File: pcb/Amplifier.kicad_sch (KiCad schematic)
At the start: 1 part, among them U6 MA12040PXUMA1

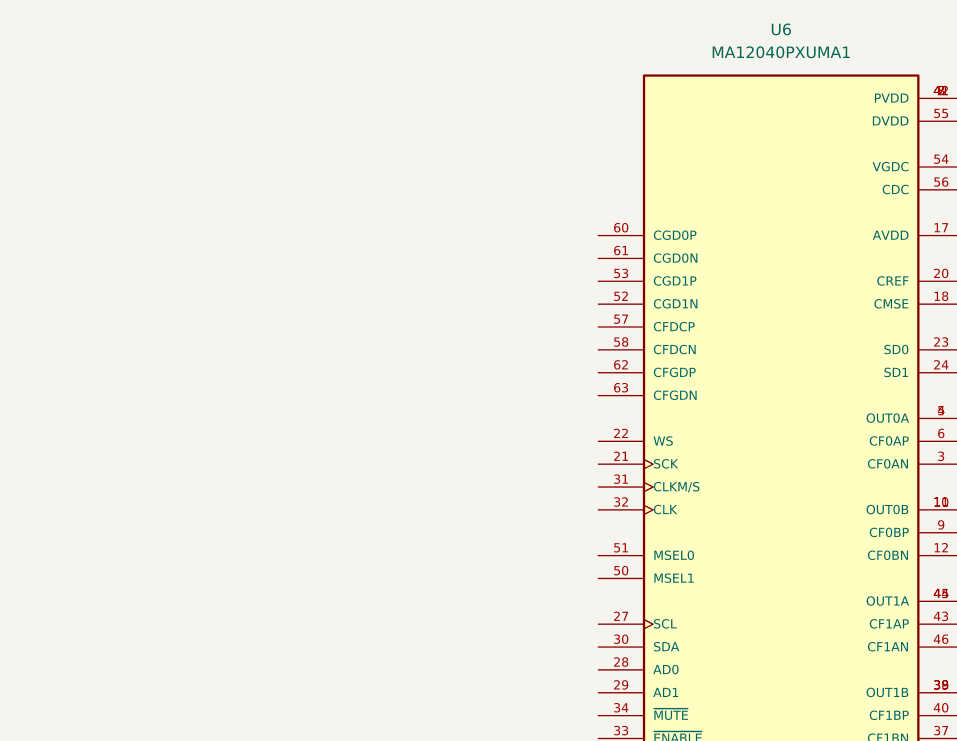
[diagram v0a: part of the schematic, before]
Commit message: - USB sound wired
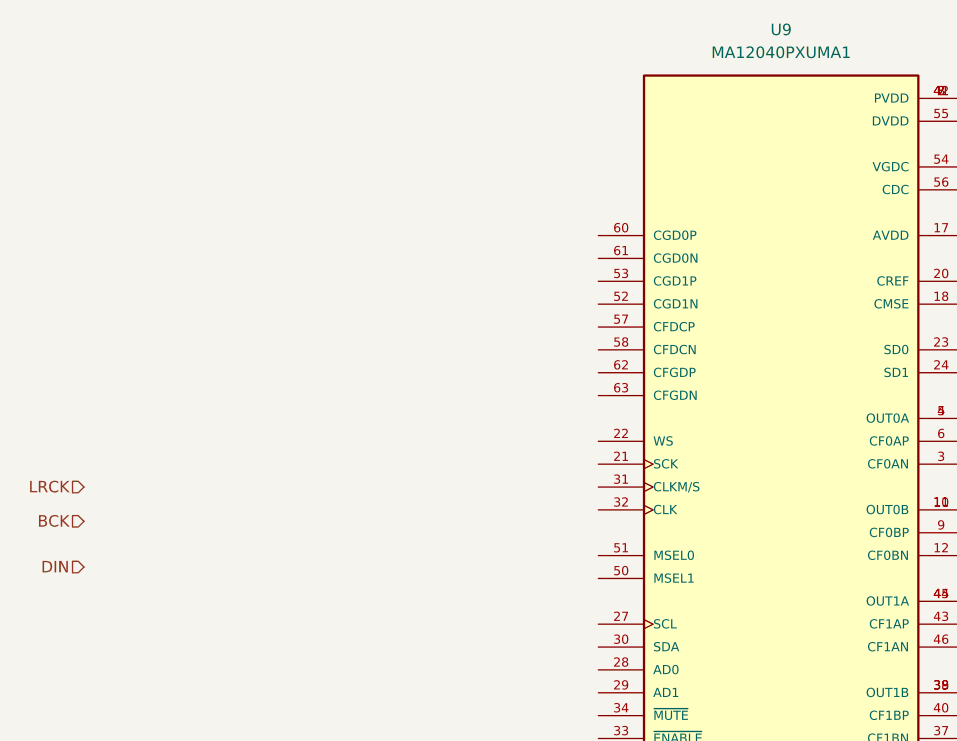
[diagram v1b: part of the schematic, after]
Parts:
- renumbered U6 to U9
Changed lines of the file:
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@@
 (kicad_sch (version 20230121) (generator eeschema)
   (paper "A4")
+  (hierarchical_label "DIN" (shape input) (at 48.26 105.41 180) (fields_autoplaced)
+    (effects (font (size 1.27 1.27)) (justify right))
+  )
+  (hierarchical_label "BCK" (shape input) (at 48.26 100.33 180) (fields_autoplaced)
+    (effects (font (size 1.27 1.27)) (justify right))
+  )
+  (hierarchical_label "LRCK" (shape input) (at 48.26 96.52 180) (fields_autoplaced)
+    (effects (font (size 1.27 1.27)) (justify right))
+  )
   (symbol (lib_id "MA12040PXUMA1:MA12040PXUMA1") (at 125.73 96.52 0) (unit 1)
     (in_bom yes) (on_board yes) (dnp no) (fields_autoplaced)
-    (property "Reference" "U6" (at 125.73 45.72 0)
+    (property "Reference" "U9" (at 125.73 45.72 0)
       (effects (font (size 1.27 1.27)))
     )
@@
       (project "VolumioAmp"
         (path "/c639bae0-d26f-43ee-9e8c-ca060284bd0b/ecbd0217-ab04-4196-9487-2acaa32ad17c"
-          (reference "U6") (unit 1)
+          (reference "U9") (unit 1)
         )
       )

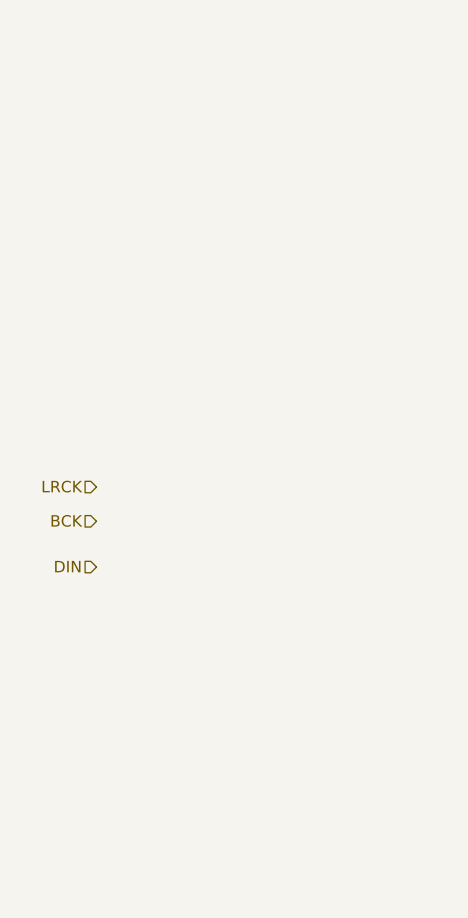
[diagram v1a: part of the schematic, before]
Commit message: WM8804 via i2c
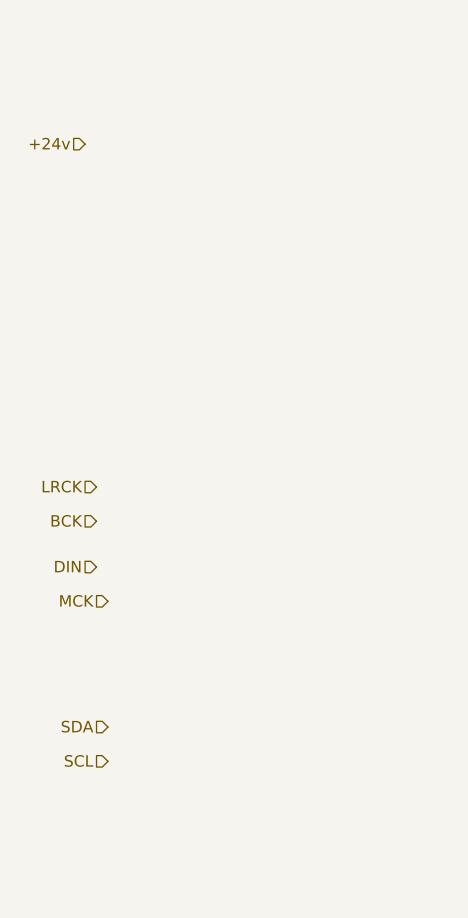
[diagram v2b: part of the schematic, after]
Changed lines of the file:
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@@
+    (effects (font (size 1.27 1.27)) (justify right))
+  )
+  (hierarchical_label "SDA" (shape input) (at 49.53 123.19 180) (fields_autoplaced)
     (effects (font (size 1.27 1.27)) (justify right))
   )
@@
     (effects (font (size 1.27 1.27)) (justify right))
   )
+  (hierarchical_label "SCL" (shape input) (at 49.53 127 180) (fields_autoplaced)
+    (effects (font (size 1.27 1.27)) (justify right))
+  )
+  (hierarchical_label "MCK" (shape input) (at 49.53 109.22 180) (fields_autoplaced)
+    (effects (font (size 1.27 1.27)) (justify right))
+  )
   (hierarchical_label "LRCK" (shape input) (at 48.26 96.52 180) (fields_autoplaced)
     (effects (font (size 1.27 1.27)) (justify right))
   )
+  (hierarchical_label "+24v" (shape input) (at 46.99 58.42 180) (fields_autoplaced)
+    (effects (font (size 1.27 1.27)) (justify right))
+  )

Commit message: - work in progress
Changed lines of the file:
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@@
 (kicad_sch (version 20230121) (generator eeschema)
   (paper "A4")
-  (hierarchical_label "DIN" (shape input) (at 48.26 105.41 180) (fields_autoplaced)
+  (bus (pts (xy 36.83 91.44) (xy 83.82 91.44))
+    (stroke (width 0) (type default))
+  )
+  (label "I2S{LRCK BCK MCK D}" (at 43.18 91.44 0) (fields_autoplaced)
+    (effects (font (size 1.27 1.27)) (justify left bottom))
+  )
+  (hierarchical_label "I2S" (shape input) (at 36.83 91.44 180) (fields_autoplaced)
     (effects (font (size 1.27 1.27)) (justify right))
   )
@@
     (effects (font (size 1.27 1.27)) (justify right))
   )
-  (hierarchical_label "BCK" (shape input) (at 48.26 100.33 180) (fields_autoplaced)
-    (effects (font (size 1.27 1.27)) (justify right))
-  )
   (hierarchical_label "SCL" (shape input) (at 49.53 127 180) (fields_autoplaced)
     (effects (font (size 1.27 1.27)) (justify right))
   )
-  (hierarchical_label "MCK" (shape input) (at 49.53 109.22 180) (fields_autoplaced)
-    (effects (font (size 1.27 1.27)) (justify right))
-  )
-  (hierarchical_label "LRCK" (shape input) (at 48.26 96.52 180) (fields_autoplaced)
-    (effects (font (size 1.27 1.27)) (justify right))
-  )

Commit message: - voor aanpassing design rules jclpcb
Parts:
- U9: footprint Libraries:QFN50P900X900X90-65N -> Footprints:QFN50P900X900X90-65N
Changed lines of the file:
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@@
       (effects (font (size 1.27 1.27)))
     )
-    (property "Footprint" "Libraries:QFN50P900X900X90-65N" (at 125.73 96.52 0)
+    (property "Footprint" "Footprints:QFN50P900X900X90-65N" (at 125.73 96.52 0)
       (effects (font (size 1.27 1.27)) (justify bottom) hide)
     )

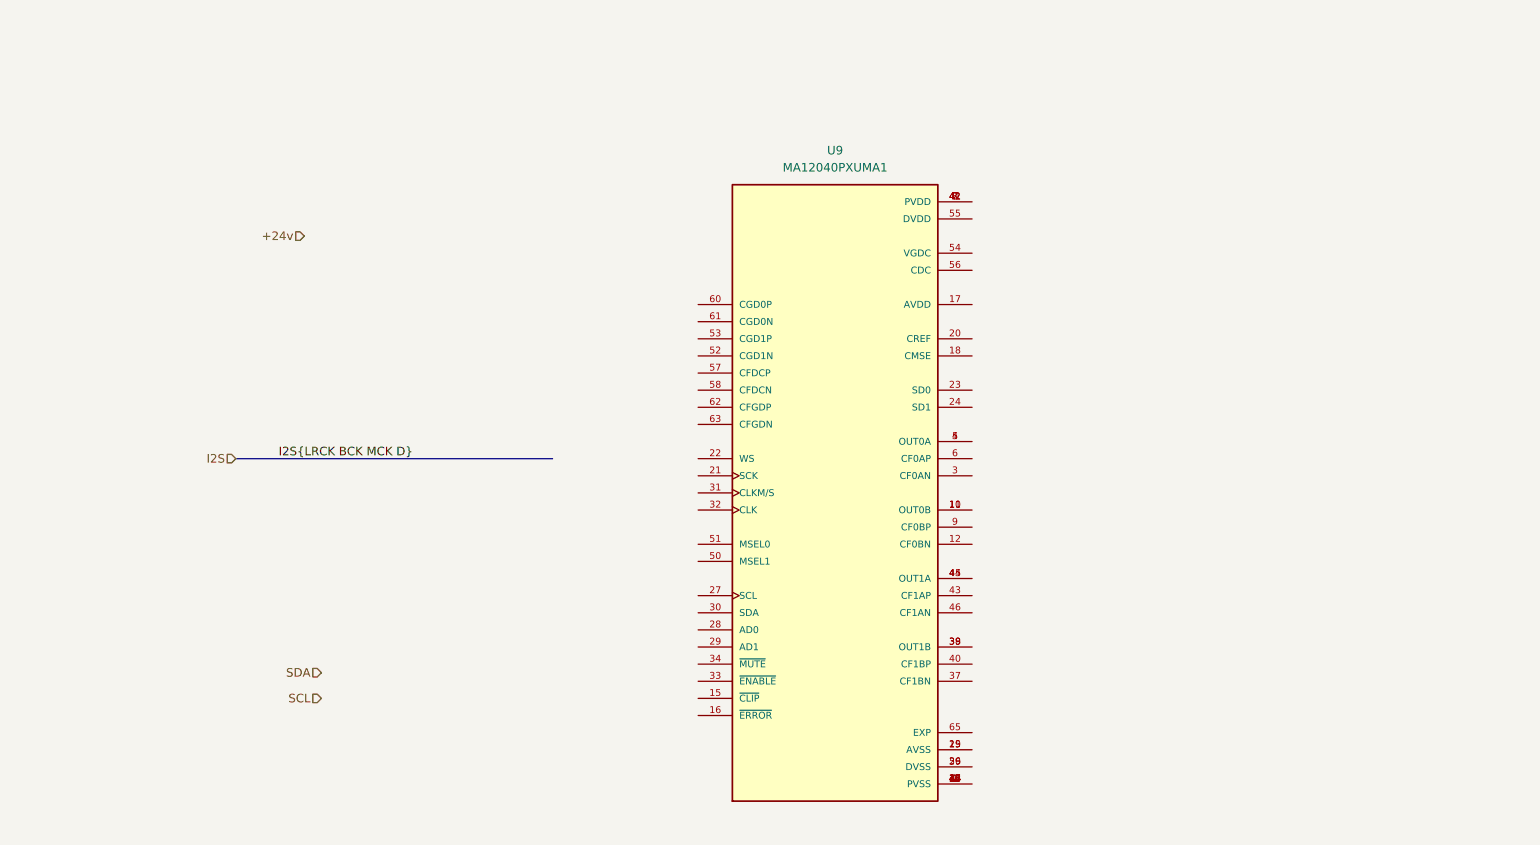
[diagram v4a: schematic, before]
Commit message: - amp connected
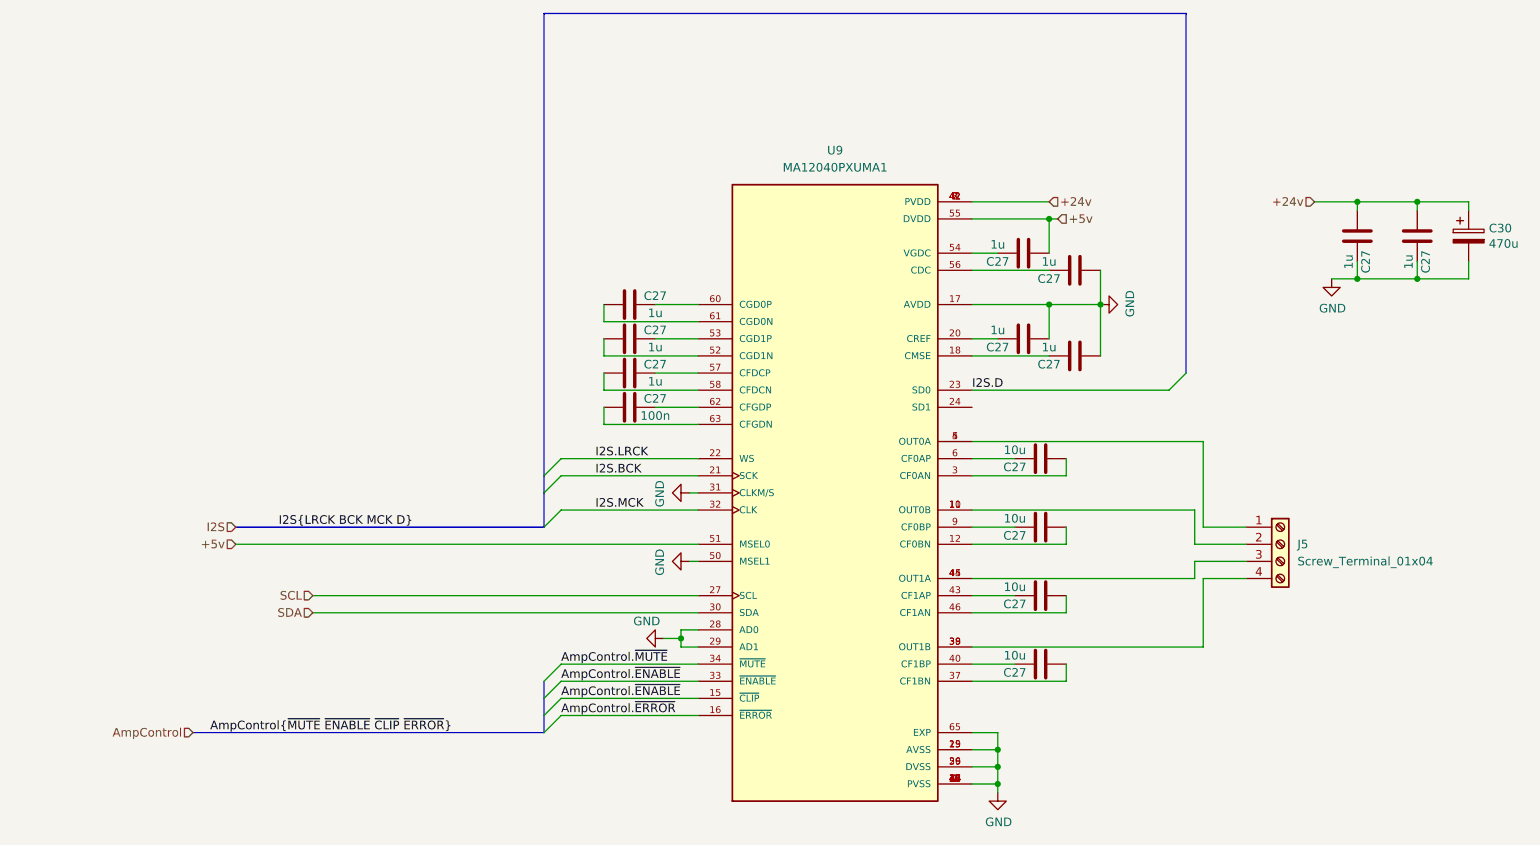
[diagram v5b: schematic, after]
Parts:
- added C27 (x9): 1u, Capacitor_SMD:C_0805_2012Metric_Pad1.18x1.45mm_HandSolder, symbol Device:C
- added C27 (x4): 10u, Capacitor_SMD:C_0805_2012Metric_Pad1.18x1.45mm_HandSolder, symbol Device:C
- added C27: 100n, Capacitor_SMD:C_0805_2012Metric_Pad1.18x1.45mm_HandSolder, symbol Device:C
- added C30: 470u, Capacitor_Tantalum_SMD:CP_EIA-7343-31_Kemet-D, symbol Device:CP
- added J5: Screw_Terminal_01x04, TerminalBlock:TerminalBlock_bornier-4_P5.08mm, symbol Connector:Screw_Terminal_01x04
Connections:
- net +24v: now also U9.41 (PVDD), U9.42 (PVDD), U9.7 (PVDD), U9.8 (PVDD), C27.2, C27.2, C30.1
- net SCL: now also U9.27 (SCL)
- net SDA: now also U9.30 (SDA)
- net GND: now reaches U9.1 (PVSS), U9.13 (PVSS), U9.14 (PVSS), U9.2 (PVSS), U9.35 (PVSS), U9.36 (PVSS), U9.47 (PVSS), U9.48 (PVSS)
- net GND: now also U9.17 (AVDD), U9.19 (AVSS), U9.25 (AVSS), U9.26 (DVSS), U9.28 (AD0), U9.29 (AD1), U9.31 (CLKM/S), U9.50 (MSEL1), U9.59 (DVSS), U9.65 (EXP), C27.1, C27.1, C27.2, C27.2, C27.2, C30.2
- net at U9.10 (OUT0B), U9.11 (OUT0B): now also J5.2 (Pin_2)
- net at U9.12 (CF0BN): now also C27.2
- net AmpControl.~{ENABLE}: now reaches U9.15 (~{CLIP})
- net AmpControl.~{ENABLE}: now also U9.33 (~{ENABLE})
- net AmpControl.~{ERROR}: now reaches U9.16 (~{ERROR})
- net at U9.18 (CMSE): now also C27.1
- net at U9.20 (CREF): now also C27.1
- net I2S.BCK: now reaches U9.21 (SCK)
- net I2S.LRCK: now reaches U9.22 (WS)
- net I2S.D: now reaches U9.23 (SD0)
- net at U9.3 (CF0AN): now also C27.2
- net I2S.MCK: now reaches U9.32 (CLK)
- net AmpControl.~{MUTE}: now reaches U9.34 (~{MUTE})
- net at U9.37 (CF1BN): now also C27.2
- net at U9.38 (OUT1B), U9.39 (OUT1B): now also J5.4 (Pin_4)
- net at U9.4 (OUT0A), U9.5 (OUT0A): now also J5.1 (Pin_1)
- net at U9.40 (CF1BP): now also C27.1
- net at U9.43 (CF1AP): now also C27.1
- net at U9.44 (OUT1A), U9.45 (OUT1A): now also J5.3 (Pin_3)
- net at U9.46 (CF1AN): now also C27.2
- net +5v: now reaches U9.51 (MSEL0)
- net +5v: now also U9.55 (DVDD), C27.2
- net at U9.52 (CGD1N): now also C27.2
- net at U9.53 (CGD1P): now also C27.1
- net at U9.54 (VGDC): now also C27.1
- net at U9.56 (CDC): now also C27.1
- net at U9.57 (CFDCP): now also C27.1
- net at U9.58 (CFDCN): now also C27.2
- net at U9.6 (CF0AP): now also C27.1
- net at U9.60 (CGD0P): now also C27.1
- net at U9.61 (CGD0N): now also C27.2
- net at U9.62 (CFGDP): now also C27.1
- net at U9.63 (CFGDN): now also C27.2
- net at U9.9 (CF0BP): now also C27.1

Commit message: - cleanup ERC errors
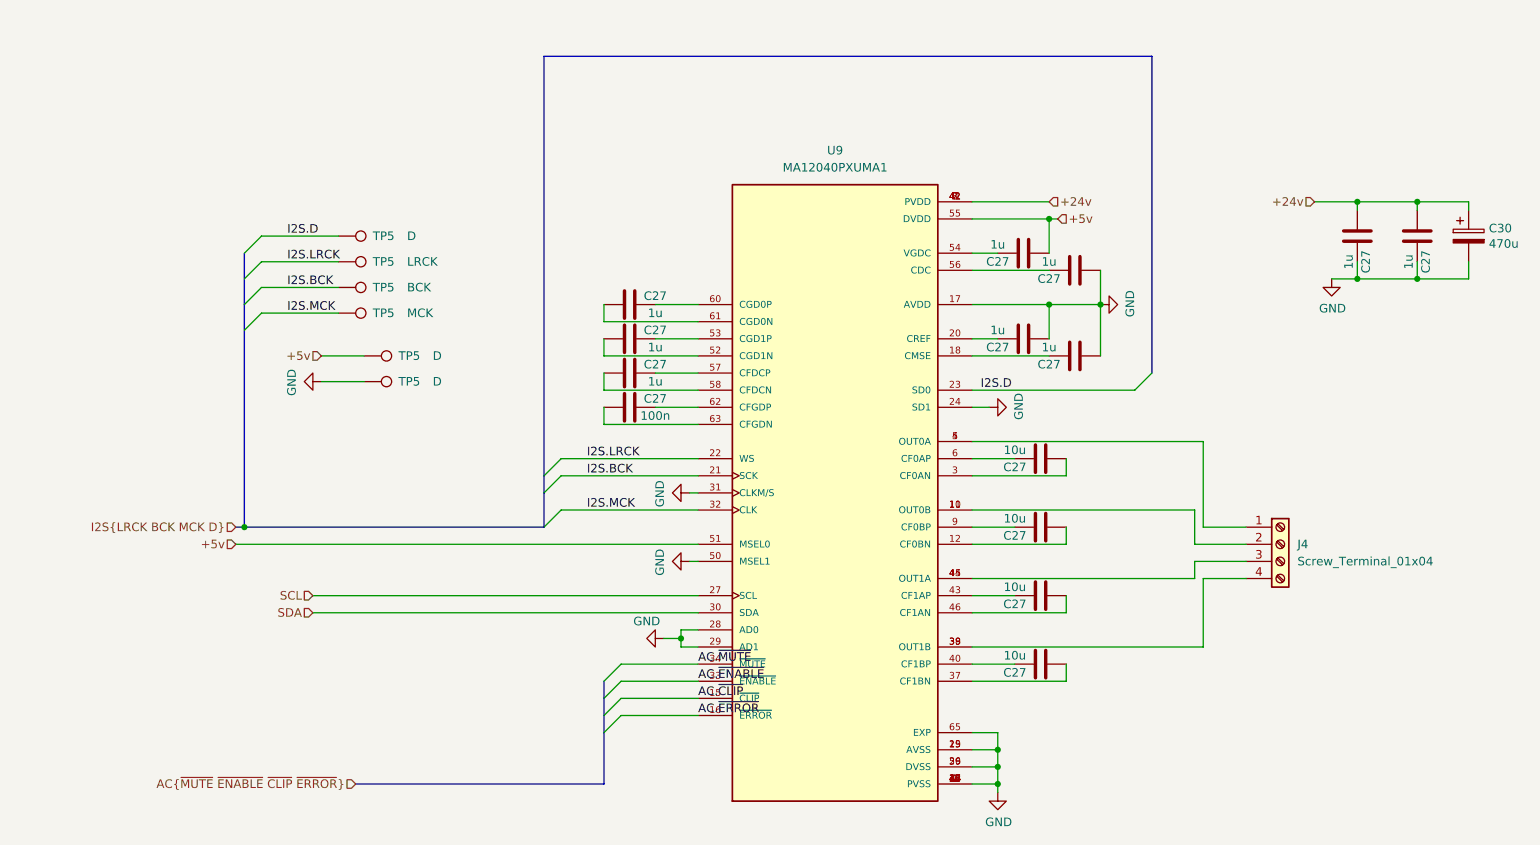
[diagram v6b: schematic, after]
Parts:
- added TP5 (x3): D, TestPoint:TestPoint_Bridge_Pitch2.54mm_Drill1.0mm, symbol Connector:TestPoint
- added TP5: MCK, TestPoint:TestPoint_Bridge_Pitch2.54mm_Drill1.0mm, symbol Connector:TestPoint
- added TP5: LRCK, TestPoint:TestPoint_Bridge_Pitch2.54mm_Drill1.0mm, symbol Connector:TestPoint
- added TP5: BCK, TestPoint:TestPoint_Bridge_Pitch2.54mm_Drill1.0mm, symbol Connector:TestPoint
- renumbered J5 to J4
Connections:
- net +5v: now also TP5.1
- net GND: now also U9.24 (SD1), TP5.1
- net I2S.BCK: now also TP5.1
- net I2S.D: now also TP5.1
- net I2S.LRCK: now also TP5.1
- net I2S.MCK: now also TP5.1
- net AmpControl.~{ENABLE} renamed AC.~{CLIP}
- net AC.~{CLIP}: no longer U9.33 (~{ENABLE})
- net AmpControl.~{ERROR} renamed AC.~{ERROR}
- net AmpControl.~{MUTE} renamed AC.~{MUTE}
- new net AC.~{ENABLE}: U9.33 (~{ENABLE})
